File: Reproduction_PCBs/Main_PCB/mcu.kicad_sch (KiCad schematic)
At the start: 35 parts, among them IC108 D78C14GF, P101 Conn_01x10, P102 Conn_01x11, P105 Conn_01x02, P107 Conn_01x02, Q105 DTC114EU3

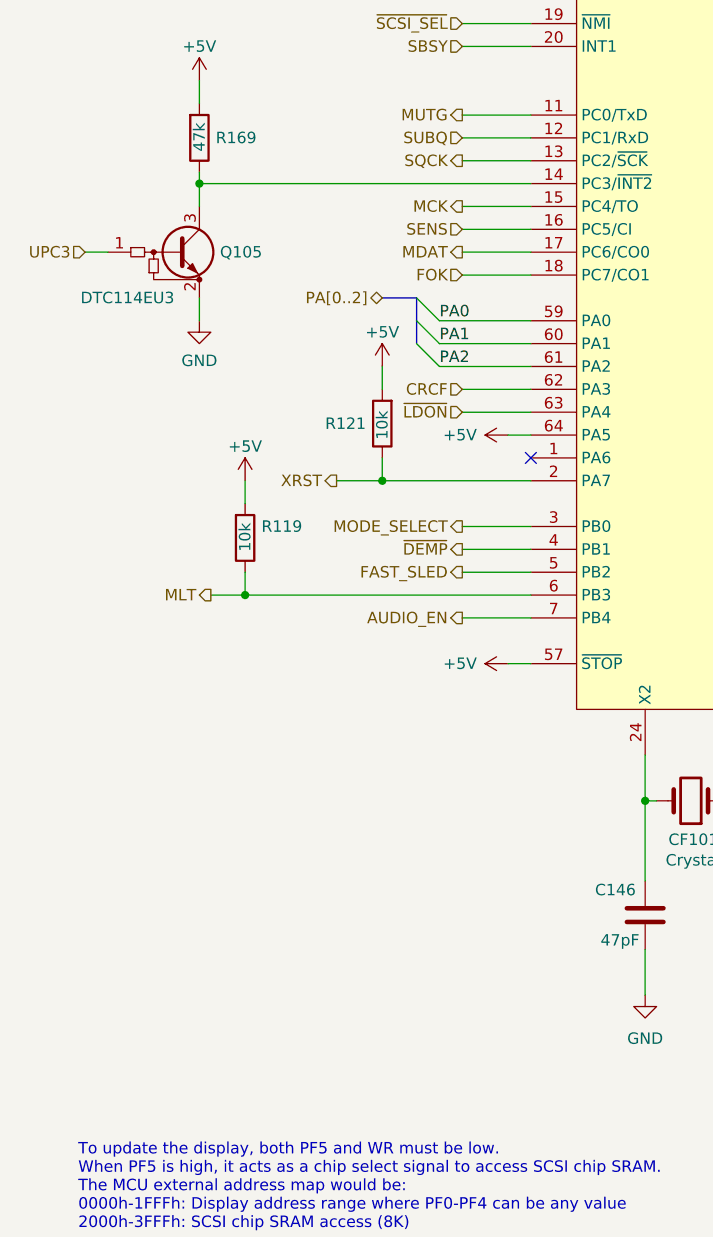
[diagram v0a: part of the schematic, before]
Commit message: Final fixes to include some ectra mounting holes + GND connection to shield
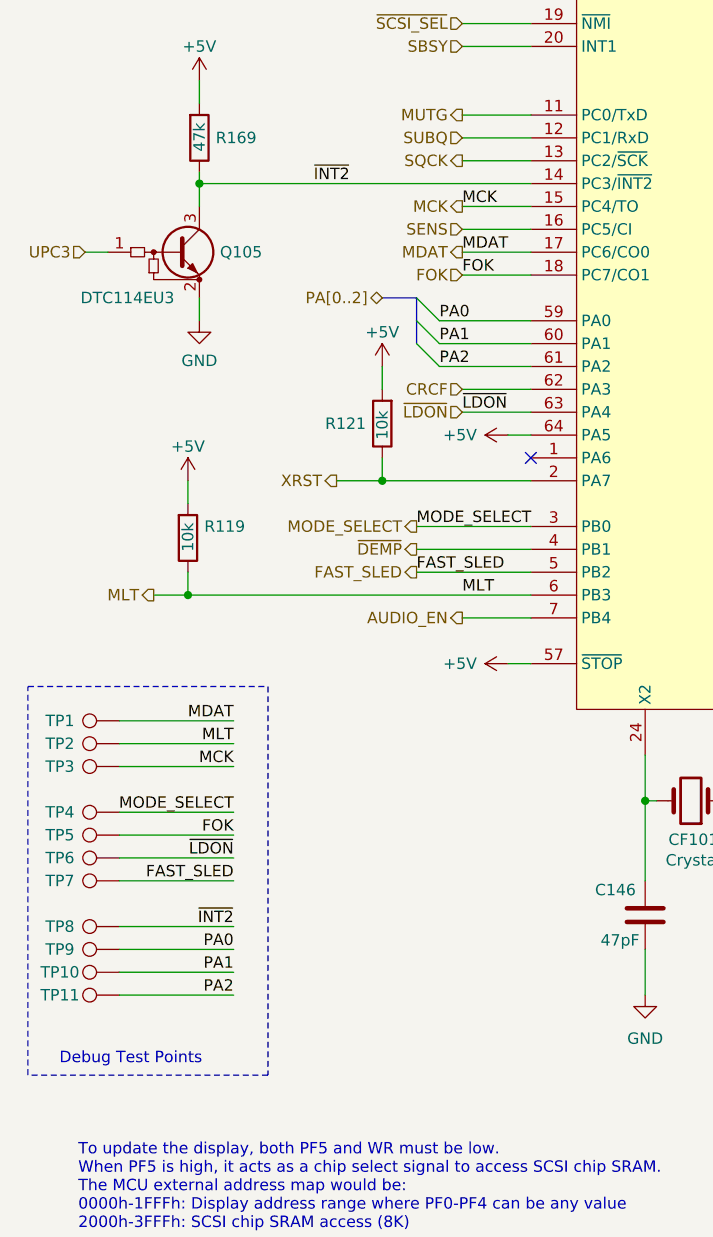
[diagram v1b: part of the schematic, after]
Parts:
- added TP1, TP10, TP11, TP2, TP3, TP4, TP5, TP6, TP7, TP8, TP9: TestPoint, TestPoint:TestPoint_Pad_D1.5mm, symbol Connector:TestPoint
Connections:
- net FAST_SLED: now also TP7.1
- net FOK: now also TP5.1
- net MCK: now also TP3.1
- net MDAT: now also TP1.1
- net MLT: now also TP2.1
- net MODE_SELECT: now also TP4.1
- net PA0: now also TP9.1
- net PA1: now also TP10.1
- net PA2: now also TP11.1
- net ~{LDON}: now also TP6.1
- net ~{INT2}: now reaches IC108.14 (PC3/~{INT2}), Q105.3 (C), R169.1
- net ~{INT2}: now also TP8.1
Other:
- note added: "Debug Test Points"
- moved on the sheet: R119
